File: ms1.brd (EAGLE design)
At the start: 160 x 100 mm, 150 parts, among them IC1 MAX3232EUE, IC2 MAX3380EEUP, J1 POWERPOLE_POWER25A, J10 Radio, J11 A3, J12 A4, J13 A5, J14 A6, J15 A7, J16 D1, J17 D2, J18 D3, J19 D4, J2 ON, J20 D5, J21 D6, J22 D7, J3 LED-EN, J4 RS232, J5 RS485, J6 A1, J7 I2C, J8 A2, J9 TTL_SERIAL, Q1 DMG6602SVT, Q2 DMG6602SVT, Q3 DMG6602SVT, Q4 DMG6602SVT, U1 LT1934ES6TRMPBF, U2 LT1934ES6TRMPBF, U3 DS3231SN, U4 ISL3179EIBZ, X1 KUSBVX-BS1N

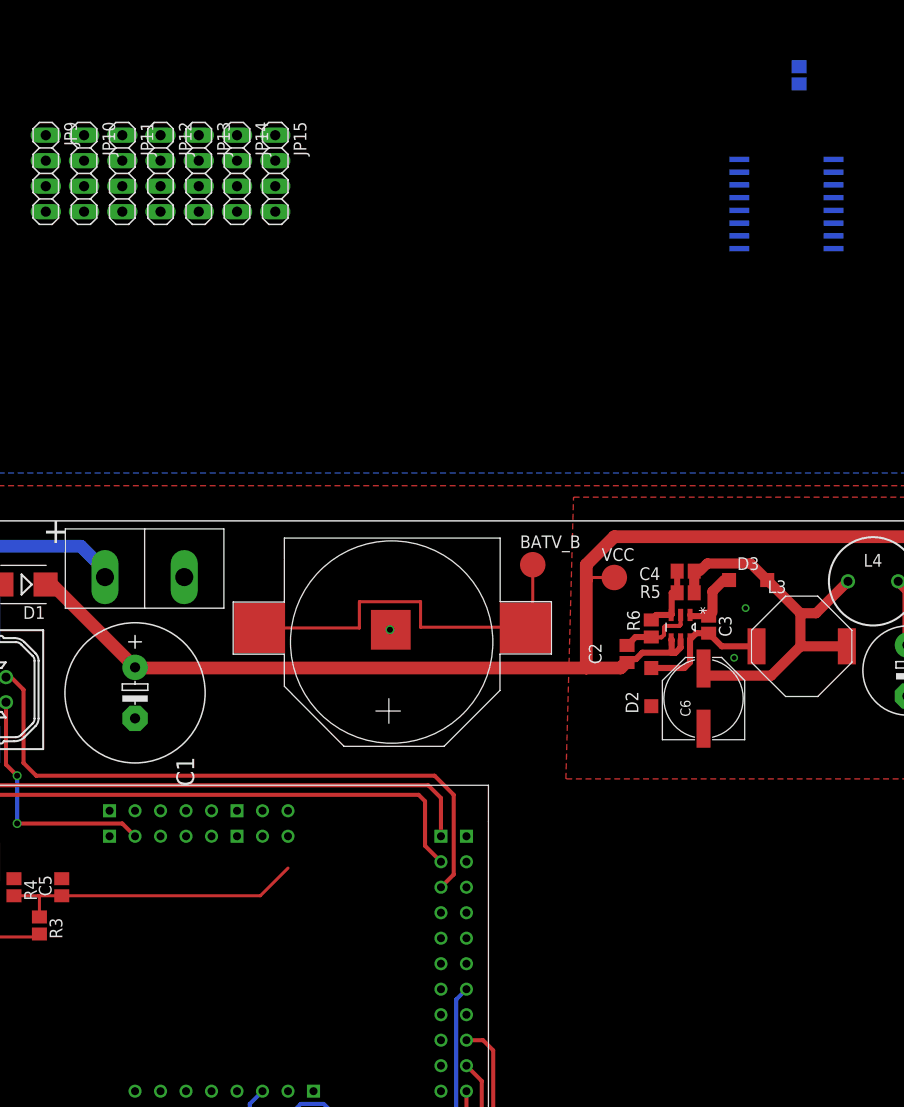
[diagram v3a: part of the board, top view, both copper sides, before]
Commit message: minor routing changes
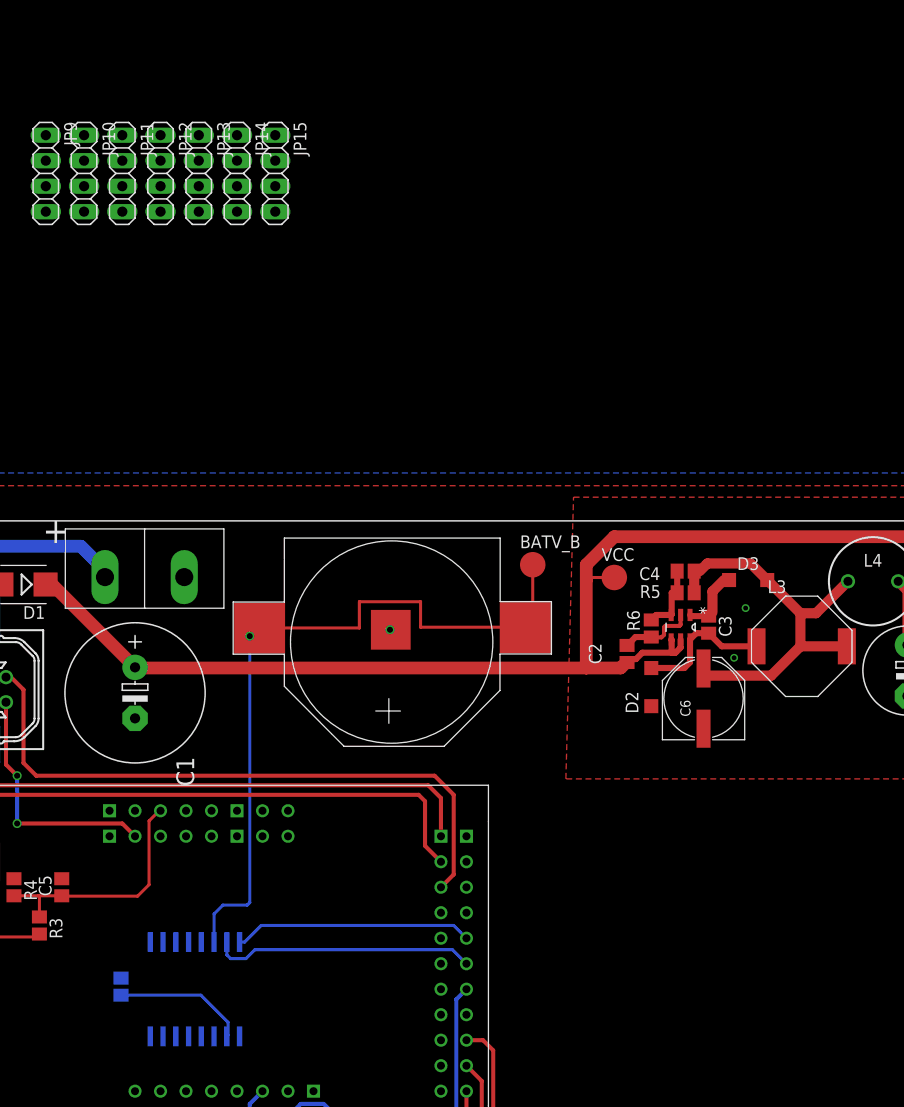
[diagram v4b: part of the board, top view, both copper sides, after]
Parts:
- moved C13 113.2 mm to (22.7, 53.6), turned to 270 degrees
- moved U3 97.9 mm to (30.1, 53.3), turned to 90 degrees
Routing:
- net VBAT_B: track 38.7 -> 73.4 mm, vias 0 -> 1
- net SDA: track 0.00 -> 26.3 mm
- net SCL: track 0.00 -> 23.8 mm
- net VCC_3V3: track 50.6 -> 63.8 mm
- net ADC_7: track 30.6 -> 24.0 mm
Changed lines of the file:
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@@
 <layer number="25" name="tNames" color="7" fill="1" visible="yes" active="yes"/>
 <layer number="26" name="bNames" color="7" fill="1" visible="yes" active="yes"/>
-<layer number="27" name="tValues" color="7" fill="1" visible="yes" active="yes"/>
-<layer number="28" name="bValues" color="7" fill="1" visible="yes" active="yes"/>
+<layer number="27" name="tValues" color="7" fill="1" visible="no" active="yes"/>
+<layer number="28" name="bValues" color="7" fill="1" visible="no" active="yes"/>
 <layer number="29" name="tStop" color="7" fill="3" visible="no" active="yes"/>
 <layer number="30" name="bStop" color="7" fill="6" visible="no" active="yes"/>
@@
 </element>
 <element name="U$2" library="z1" package="Z1" value="Z1" x="3.81" y="73.66"/>
-<element name="U3" library="farnell-parts" package="SOIC127P1032X265-16N" value="DS3231SN" x="89.027" y="131.572" rot="MR180">
-<attribute name="PACKAGE" value="SOIC-16" x="184.277" y="195.072" size="1.778" layer="28" rot="MR180" display="off"/>
-<attribute name="OC_NEWARK" value="68K3406" x="184.277" y="195.072" size="1.778" layer="28" rot="MR180" display="off"/>
-<attribute name="MPN" value="DS3231SN#" x="184.277" y="195.072" size="1.778" layer="28" rot="MR180" display="off"/>
-<attribute name="SUPPLIER" value="Maxim" x="184.277" y="195.072" size="1.778" layer="28" rot="MR180" display="off"/>
-<attribute name="OC_FARNELL" value="1593292" x="184.277" y="195.072" size="1.778" layer="28" rot="MR180" display="off"/>
-</element>
-<element name="C13" library="resistor" package="C0805" value="100nF" x="90.297" y="144.399" rot="MR90"/>
+<element name="U3" library="farnell-parts" package="SOIC127P1032X265-16N" value="DS3231SN" x="30.099" y="53.34" rot="MR90">
+<attribute name="PACKAGE" value="SOIC-16" x="-33.401" y="148.59" size="1.778" layer="28" rot="MR90" display="off"/>
+<attribute name="OC_NEWARK" value="68K3406" x="-33.401" y="148.59" size="1.778" layer="28" rot="MR90" display="off"/>
+<attribute name="MPN" value="DS3231SN#" x="-33.401" y="148.59" size="1.778" layer="28" rot="MR90" display="off"/>
+<attribute name="SUPPLIER" value="Maxim" x="-33.401" y="148.59" size="1.778" layer="28" rot="MR90" display="off"/>
+<attribute name="OC_FARNELL" value="1593292" x="-33.401" y="148.59" size="1.778" layer="28" rot="MR90" display="off"/>
+</element>
+<element name="C13" library="resistor" package="C0805" value="100nF" x="22.733" y="53.594" rot="MR270"/>
 <element name="U$1" library="gumsense" package="CR2016" value="BUTTON_CELL_NEW" x="51.308" y="80.518"/>
 <element name="U$4" library="wasp" package="WASP" value="WASP" x="124.841" y="36.068" rot="R90"/>
@@
 <contactref element="C29" pad="2"/>
 <via x="104.902" y="93.599" extent="1-16" drill="0.4826" shape="square"/>
-<wire x1="93.726" y1="136.017" x2="90.297" y2="143.549" width="0" layer="19" extent="16-16"/>
-<wire x1="93.726" y1="134.747" x2="93.726" y2="136.017" width="0" layer="19" extent="16-16"/>
-<wire x1="93.726" y1="133.477" x2="93.726" y2="134.747" width="0" layer="19" extent="16-16"/>
-<wire x1="93.726" y1="132.207" x2="93.726" y2="133.477" width="0" layer="19" extent="16-16"/>
-<wire x1="93.726" y1="130.937" x2="93.726" y2="132.207" width="0" layer="19" extent="16-16"/>
-<wire x1="84.328" y1="134.747" x2="93.726" y2="134.747" width="0" layer="19" extent="16-16"/>
-<wire x1="84.328" y1="136.017" x2="84.328" y2="134.747" width="0" layer="19" extent="16-16"/>
-<wire x1="84.328" y1="133.477" x2="84.328" y2="134.747" width="0" layer="19" extent="16-16"/>
-<wire x1="84.328" y1="132.207" x2="84.328" y2="133.477" width="0" layer="19" extent="16-16"/>
-<wire x1="104.902" y1="93.599" x2="93.726" y2="130.937" width="0" layer="19" extent="16-16"/>
+<wire x1="25.654" y1="58.039" x2="22.733" y2="54.444" width="0" layer="19" extent="16-16"/>
+<wire x1="26.924" y1="58.039" x2="25.654" y2="58.039" width="0" layer="19" extent="16-16"/>
+<wire x1="28.194" y1="58.039" x2="26.924" y2="58.039" width="0" layer="19" extent="16-16"/>
+<wire x1="29.464" y1="58.039" x2="28.194" y2="58.039" width="0" layer="19" extent="16-16"/>
+<wire x1="30.734" y1="58.039" x2="29.464" y2="58.039" width="0" layer="19" extent="16-16"/>
+<wire x1="26.924" y1="48.641" x2="26.924" y2="58.039" width="0" layer="19" extent="16-16"/>
+<wire x1="25.654" y1="48.641" x2="26.924" y2="48.641" width="0" layer="19" extent="16-16"/>
+<wire x1="28.194" y1="48.641" x2="26.924" y2="48.641" width="0" layer="19" extent="16-16"/>
+<wire x1="29.464" y1="48.641" x2="28.194" y2="48.641" width="0" layer="19" extent="16-16"/>
+<wire x1="104.902" y1="93.599" x2="30.734" y2="58.039" width="0" layer="19" extent="16-16"/>
 <wire x1="-85.979" y1="97.663" x2="2.794" y2="64.516" width="0" layer="19" extent="1-1"/>
 <wire x1="-93.599" y1="97.663" x2="-85.979" y2="97.663" width="0" layer="19" extent="1-1"/>
@@
 <wire x1="107.638" y1="87.503" x2="107.638" y2="83.116" width="0.6096" layer="1"/>
 <wire x1="107.638" y1="83.116" x2="110.156" y2="80.598" width="0.6096" layer="1"/>
-<wire x1="84.328" y1="128.397" x2="90.297" y2="145.249" width="0" layer="19" extent="16-16"/>
-<wire x1="107.638" y1="87.503" x2="84.328" y2="128.397" width="0" layer="19" extent="1-16"/>
+<wire x1="107.638" y1="87.503" x2="33.274" y2="48.641" width="0" layer="19" extent="1-16"/>
 <wire x1="57.15" y1="63.5" x2="107.638" y2="83.116" width="0" layer="19" extent="1-1"/>
 <wire x1="-160.02" y1="136.31" x2="41.91" y2="40.64" width="0" layer="19" extent="1-1"/>
@@
 <wire x1="-221.9928" y1="104.517" x2="-221.9928" y2="105.167" width="0" layer="19" extent="1-1"/>
 <wire x1="-224.282" y1="104.609" x2="-221.9928" y2="104.517" width="0" layer="19" extent="1-1"/>
+<wire x1="22.733" y1="52.744" x2="30.695" y2="52.744" width="0.3048" layer="16"/>
+<wire x1="30.695" y1="52.744" x2="33.401" y2="50.038" width="0.3048" layer="16"/>
+<wire x1="33.401" y1="50.038" x2="33.401" y2="48.768" width="0.3048" layer="16"/>
+<wire x1="33.401" y1="48.768" x2="33.274" y2="48.641" width="0.3048" layer="16"/>
 </signal>
 <signal name="N$1">
@@
 <wire x1="52.578" y1="89.408" x2="63.008" y2="89.408" width="0.3048" layer="1"/>
 <wire x1="63.008" y1="89.408" x2="63.008" y2="89.348" width="0.3048" layer="1"/>
-<wire x1="63.754" y1="95.631" x2="93.726" y2="129.667" width="0" layer="19" extent="1-16"/>
+<wire x1="36.543" y1="89.3305" x2="36.3715" y2="89.3305" width="0.3048" layer="1"/>
+<wire x1="36.3715" y1="89.3305" x2="35.56" y2="88.519" width="0.3048" layer="1"/>
+<via x="35.56" y="88.519" extent="1-16" drill="0.6" shape="square"/>
+<wire x1="35.56" y1="88.519" x2="35.56" y2="61.976" width="0.3048" layer="16"/>
+<wire x1="35.56" y1="61.976" x2="35.306" y2="61.722" width="0.3048" layer="16"/>
+<wire x1="35.306" y1="61.722" x2="32.893" y2="61.722" width="0.3048" layer="16"/>
+<wire x1="32.893" y1="61.722" x2="32.004" y2="60.833" width="0.3048" layer="16"/>
+<wire x1="32.004" y1="60.833" x2="32.004" y2="58.039" width="0.3048" layer="16"/>
 </signal>
 <signal name="N$7">
@@
 <contactref element="U$4" pad="S24"/>
 <contactref element="J7" pad="3"/>
-<wire x1="57.15" y1="58.42" x2="93.726" y2="127.127" width="0" layer="19" extent="16-16"/>
 <wire x1="4.953" y1="9.017" x2="57.15" y2="58.42" width="0" layer="19" extent="1-1"/>
 <wire x1="140.081" y1="5.588" x2="57.15" y2="58.42" width="0" layer="19" extent="1-1"/>
+<wire x1="34.544" y1="58.039" x2="35.052" y2="58.039" width="0.3048" layer="16"/>
+<wire x1="35.052" y1="58.039" x2="36.703" y2="59.69" width="0.3048" layer="16"/>
+<wire x1="36.703" y1="59.69" x2="55.88" y2="59.69" width="0.3048" layer="16"/>
+<wire x1="55.88" y1="59.69" x2="57.15" y2="58.42" width="0.3048" layer="16"/>
 </signal>
 <signal name="SDA">
@@
 <contactref element="U$4" pad="S23"/>
 <contactref element="J7" pad="2"/>
-<wire x1="57.15" y1="55.88" x2="93.726" y2="128.397" width="0" layer="19" extent="16-16"/>
 <wire x1="4.953" y1="6.477" x2="57.15" y2="55.88" width="0" layer="19" extent="1-1"/>
 <wire x1="140.081" y1="3.048" x2="57.15" y2="55.88" width="0" layer="19" extent="1-1"/>
+<wire x1="33.274" y1="58.039" x2="33.274" y2="56.769" width="0.3048" layer="16"/>
+<wire x1="33.274" y1="56.769" x2="33.655" y2="56.388" width="0.3048" layer="16"/>
+<wire x1="33.655" y1="56.388" x2="35.179" y2="56.388" width="0.3048" layer="16"/>
+<wire x1="35.179" y1="56.388" x2="36.068" y2="57.277" width="0.3048" layer="16"/>
+<wire x1="36.068" y1="57.277" x2="55.753" y2="57.277" width="0.3048" layer="16"/>
+<wire x1="55.753" y1="57.277" x2="57.15" y2="55.88" width="0.3048" layer="16"/>
 </signal>
 <signal name="SPI_CLK">
@@
 <wire x1="14.605" y1="60.54" x2="14.605" y2="62.523" width="0.3048" layer="1"/>
 <wire x1="14.605" y1="62.523" x2="14.478" y2="62.65" width="0.3048" layer="1"/>
-<wire x1="16.8275" y1="62.65" x2="36.615" y2="62.65" width="0.3048" layer="1"/>
-<wire x1="36.615" y1="62.65" x2="39.37" y2="65.405" width="0.3048" layer="1"/>
-<wire x1="16.8275" y1="62.65" x2="26.67" y2="71.12" width="0" layer="19" extent="1-1"/>
+<wire x1="26.67" y1="71.12" x2="26.543" y2="71.12" width="0.3048" layer="1"/>
+<wire x1="26.543" y1="71.12" x2="25.527" y2="70.104" width="0.3048" layer="1"/>
+<wire x1="25.527" y1="70.104" x2="25.527" y2="63.754" width="0.3048" layer="1"/>
+<wire x1="25.527" y1="63.754" x2="24.384" y2="62.611" width="0.3048" layer="1"/>
+<wire x1="24.384" y1="62.611" x2="16.8665" y2="62.611" width="0.3048" layer="1"/>
+<wire x1="16.8665" y1="62.611" x2="16.8275" y2="62.65" width="0.3048" layer="1"/>
 </signal>
 <signal name="WADC_4">

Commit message: more routing - mainly digital signals
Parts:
- moved R30 304.8 mm to (100.8, 77.9), turned to 0 degrees
- moved LED15 302.2 mm to (97.7, 75.8), turned to 90 degrees
- moved J4 33.5 mm to (-140.5, 84.5)
- moved JP1 24.0 mm to (15.3, 67.5), turned to 180 degrees
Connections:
- net AY renamed RS485_P
- net BZ renamed RS485_N
- net USB_D+ renamed USB_D_P
- net USB_D- renamed USB_D_N
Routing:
- net SENSE_EN: track 12.2 -> 222.9 mm, vias 2 -> 5
- net VCC_3V3: track 63.8 -> 162.2 mm, vias 1 -> 3
- net SCL: track 23.8 -> 113.1 mm, vias 0 -> 2
- net SDA: track 26.3 -> 110.4 mm, vias 0 -> 2
- net BATV_EN: track 15.1 -> 19.5 mm
- net USB_D_P: track 67.3 -> 64.3 mm
- net N$51: track 0.00 -> 2.56 mm
- net USB_D_N: track 63.5 -> 64.3 mm
- net SENSE_3V3: track 308.8 -> 308.3 mm

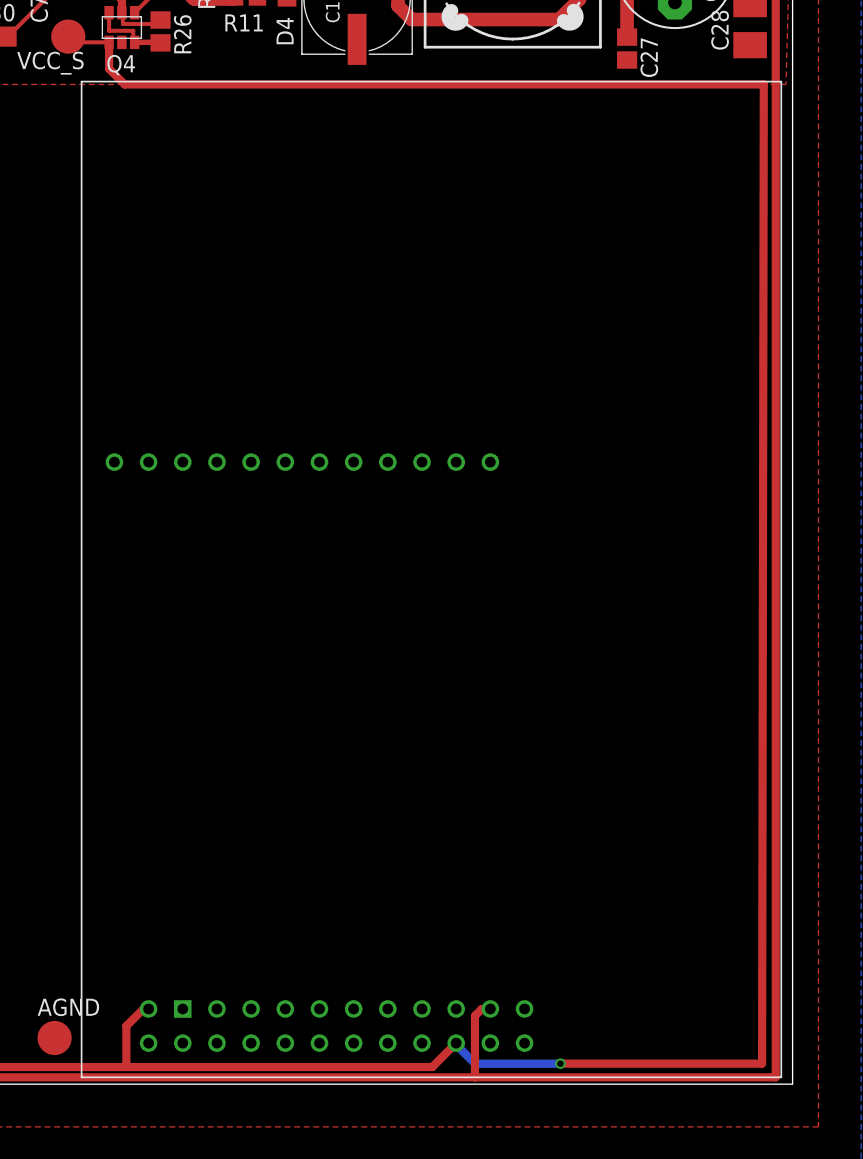
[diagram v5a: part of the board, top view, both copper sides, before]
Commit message: removal of libellium part
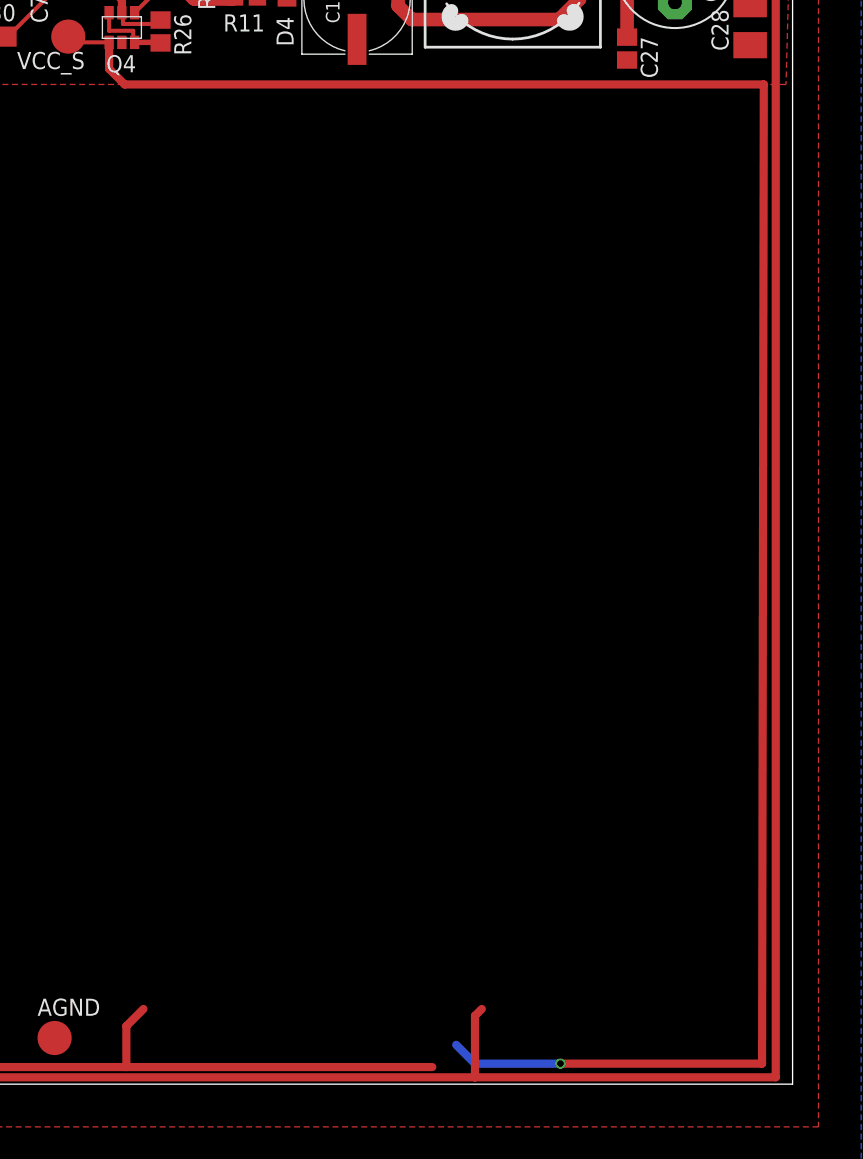
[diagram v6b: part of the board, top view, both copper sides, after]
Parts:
- removed U$4: WASP, wasp:WASP
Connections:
- removed net WADC_7: U$4.S14
- net GND: no longer U$4.A6, U$4.S4
- net SCL: no longer U$4.S24
- net SDA: no longer U$4.S23
- net SENSE_3V3: no longer U$4.A10, U$4.S19, U$4.S2
- net SENSE_5V: no longer U$4.S22
- net SPI_CLK: no longer U$4.A7
- net SPI_SIMO: no longer U$4.A11
- net SPI_SOMI: no longer U$4.A12
- net WADC_1: no longer U$4.S20
- net WADC_2: no longer U$4.S17
- net WADC_3: no longer U$4.S18
- net WADC_4: no longer U$4.S15
- net WADC_5: no longer U$4.S16
- net WADC_6: no longer U$4.S13
- net WDIO_1: no longer U$4.S12
- net WDIO_2: no longer U$4.S9
- net WDIO_3: no longer U$4.S10
- net WDIO_4: no longer U$4.S7
- net WDIO_5: no longer U$4.S8
- net WDIO_6: no longer U$4.S5
- net WDIO_7: no longer U$4.S6
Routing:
- net SENSE_3V3: track 308.3 -> 305.2 mm
- net SENSE_5V: track 269.4 -> 268.8 mm
